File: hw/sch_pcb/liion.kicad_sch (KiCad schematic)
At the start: 67 parts, among them Q4 BC817-25, Q7 BSS83P, U1 BQ34Z100, U13 BQ25628E, U2 SN74HC164P

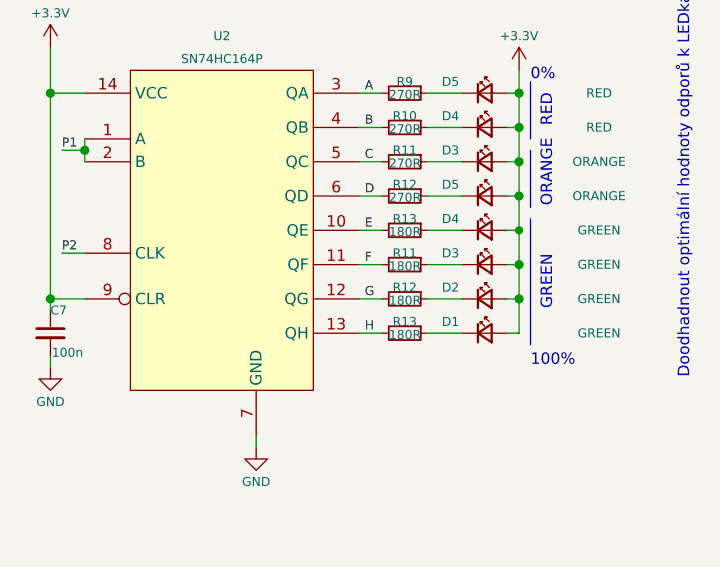
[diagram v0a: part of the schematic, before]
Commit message: Update components values to tested ones.
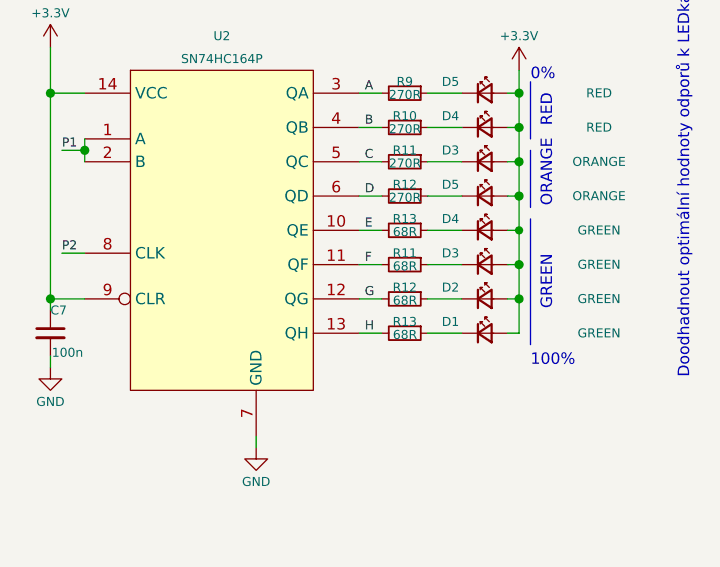
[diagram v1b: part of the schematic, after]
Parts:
- R11, R12, R13: value 180R -> 68R; UST_ID 5c70984512875079b91f897c -> 5c70984512875079b91f8975
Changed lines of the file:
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@@
       (effects (font (size 1 1)))
     )
-    (property "Value" "180R" (at 245.1354 130.9878 90)
+    (property "Value" "68R" (at 245.1354 130.9878 90)
       (effects (font (size 1 1)))
     )
@@
       (effects (font (size 1 1)) hide)
     )
-    (property "UST_ID" "5c70984512875079b91f897c" (at 245.11 130.81 0)
+    (property "UST_ID" "5c70984512875079b91f8975" (at 245.11 130.81 0)
       (effects (font (size 1.27 1.27)) hide)
     )
@@
       (effects (font (size 1 1)))
     )
-    (property "Value" "180R" (at 245.1354 134.7978 90)
+    (property "Value" "68R" (at 245.1354 134.7978 90)
       (effects (font (size 1 1)))
     )
@@
       (effects (font (size 1 1)) hide)
     )
-    (property "UST_ID" "5c70984512875079b91f897c" (at 245.11 134.62 0)
+    (property "UST_ID" "5c70984512875079b91f8975" (at 245.11 134.62 0)
       (effects (font (size 1.27 1.27)) hide)
     )
@@
       (effects (font (size 1 1)))
     )
-    (property "Value" "180R" (at 245.1354 142.4178 90)
+    (property "Value" "68R" (at 245.1354 142.4178 90)
       (effects (font (size 1 1)))
     )
@@
       (effects (font (size 1 1)) hide)
     )
-    (property "UST_ID" "5c70984512875079b91f897c" (at 245.11 142.24 0)
+    (property "UST_ID" "5c70984512875079b91f8975" (at 245.11 142.24 0)
       (effects (font (size 1.27 1.27)) hide)
     )
@@
       (effects (font (size 1 1)))
     )
-    (property "Value" "180R" (at 245.1354 138.6078 90)
+    (property "Value" "68R" (at 245.1354 138.6078 90)
       (effects (font (size 1 1)))
     )
@@
       (effects (font (size 1 1)) hide)
     )
-    (property "UST_ID" "5c70984512875079b91f897c" (at 245.11 138.43 0)
+    (property "UST_ID" "5c70984512875079b91f8975" (at 245.11 138.43 0)
       (effects (font (size 1.27 1.27)) hide)
     )

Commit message: Fix UST_ID.
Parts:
- R51: value 270R -> 68R; UST_ID 5c70984512875079b91f8983 -> 5c70984512875079b91f8975
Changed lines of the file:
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@@
       (effects (font (size 1 1)))
     )
-    (property "Value" "270R" (at 46.99 86.36 90)
+    (property "Value" "68R" (at 46.99 86.36 90)
       (effects (font (size 1 1)))
     )
@@
       (effects (font (size 1 1)) hide)
     )
-    (property "UST_ID" "5c70984512875079b91f8983" (at 46.99 86.36 0)
+    (property "UST_ID" "5c70984512875079b91f8975" (at 46.99 86.36 0)
       (effects (font (size 1.27 1.27)) hide)
     )

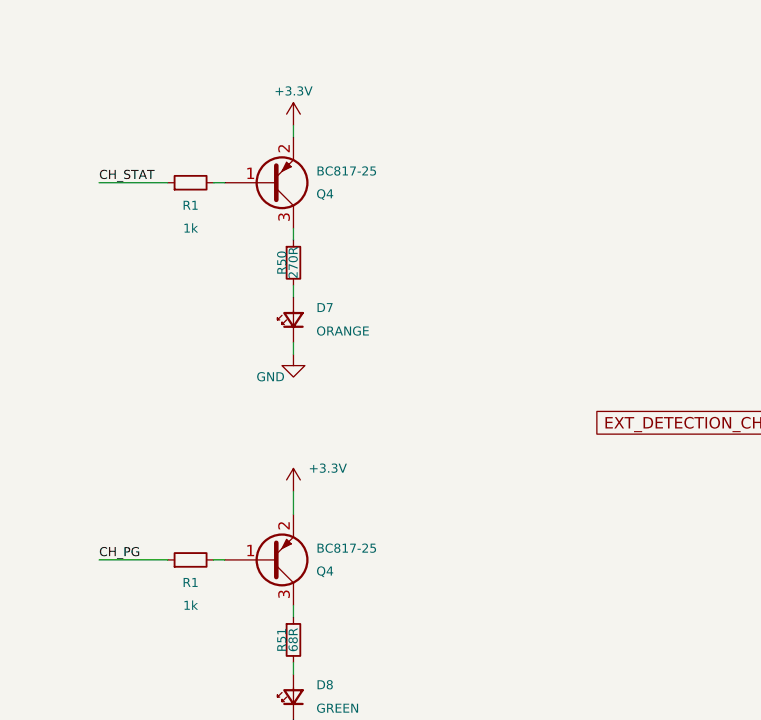
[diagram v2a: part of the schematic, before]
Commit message: Update and correct values from manufacturing process.
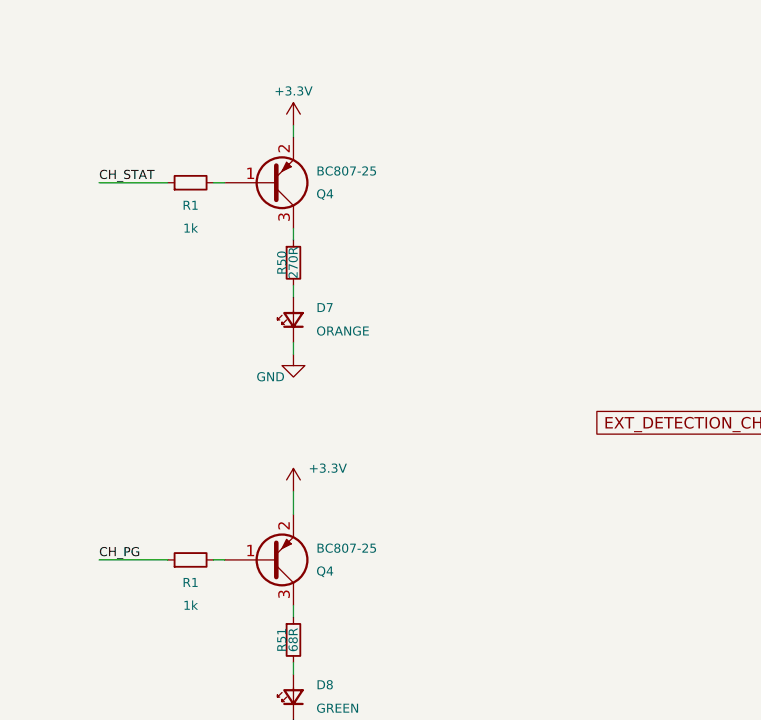
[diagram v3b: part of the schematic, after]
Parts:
- Q4: value BC817-25 -> BC807-25
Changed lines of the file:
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@@
       (effects (font (size 1 1)) (justify left))
     )
-    (property "Value" "BC817-25" (at 49.53 76.2 0)
+    (property "Value" "BC807-25" (at 49.53 76.2 0)
       (effects (font (size 1 1)) (justify left))
     )
@@
       (effects (font (size 1 1)) (justify left))
     )
-    (property "Value" "BC817-25" (at 49.53 34.29 0)
-      (effects (font (size 1 1)) (justify left))
-    )
+    (property "Value" "BC807-25" (at 49.53 34.29 0)
+      (effects (font (size 1 1)) (justify left))
+    )

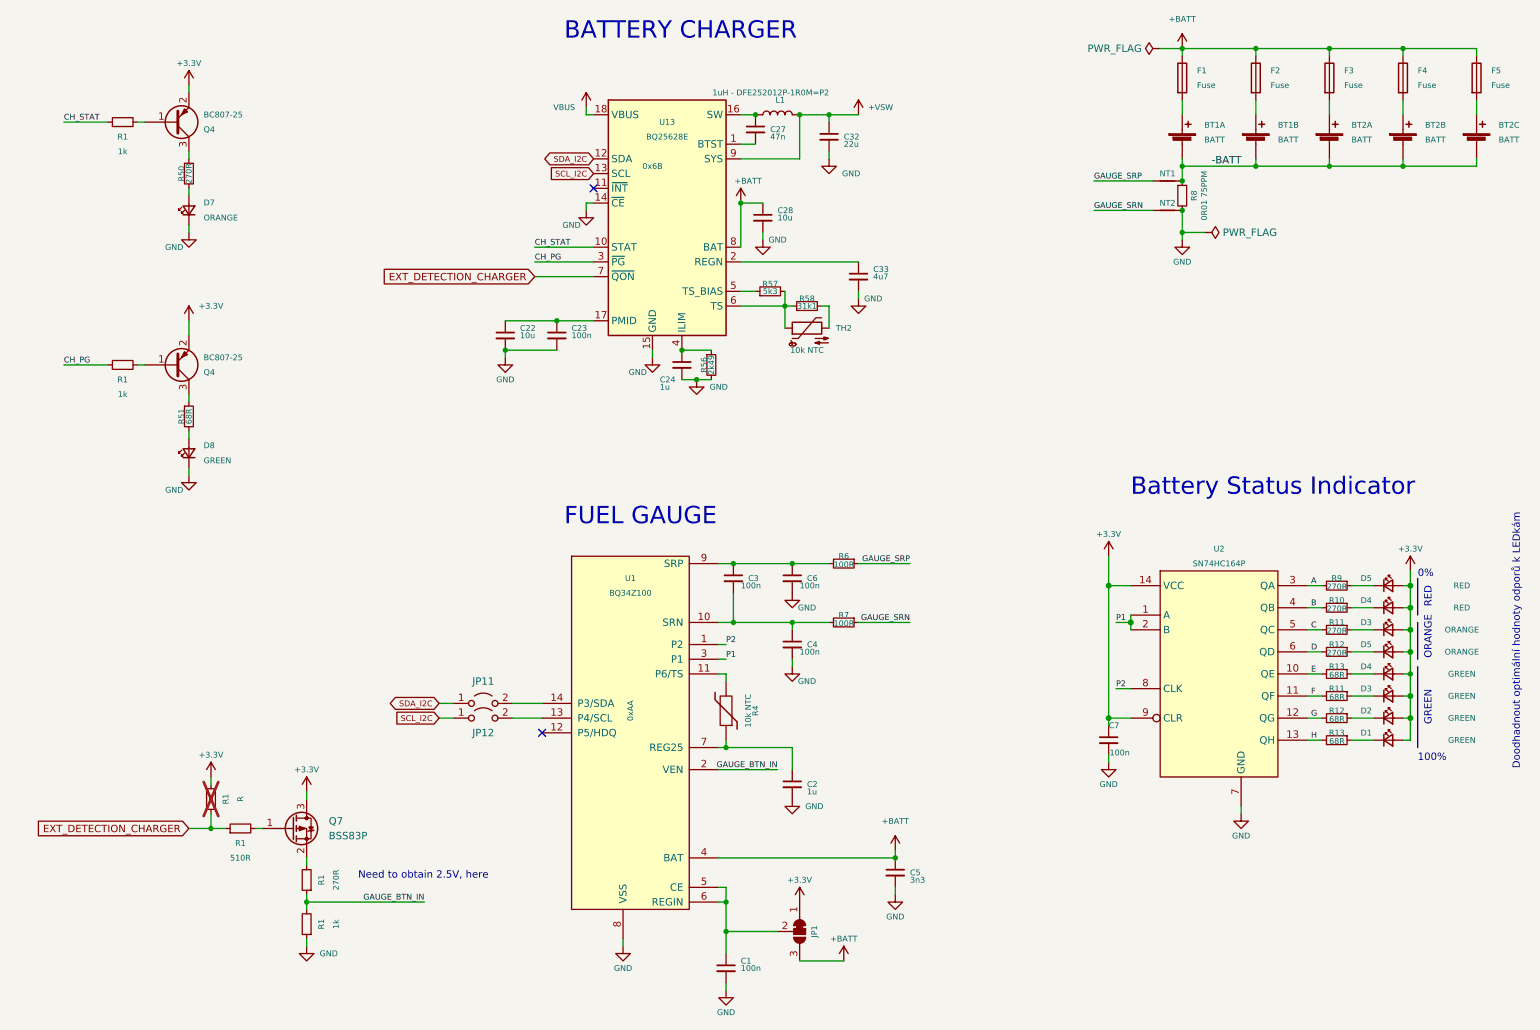
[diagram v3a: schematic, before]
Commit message: Update the commponent values according to actual component values used during manufacturing.
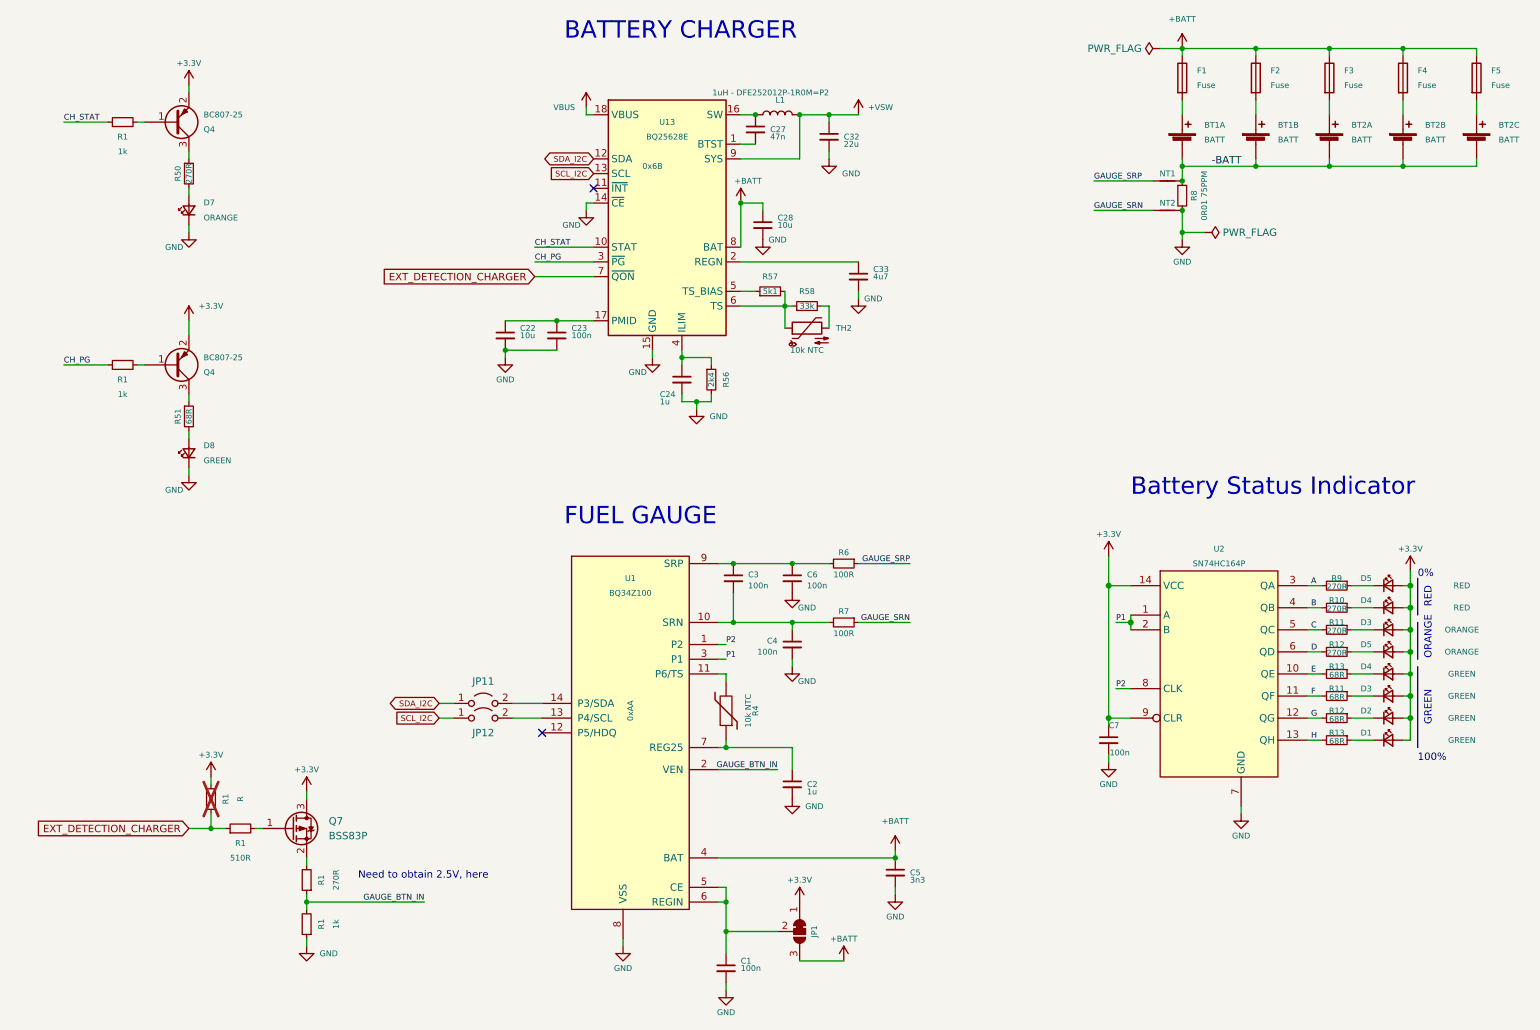
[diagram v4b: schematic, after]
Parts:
- R56: value 2k49 -> 2k4
- R57: value 5k3 -> 5k1
- R58: value 31k1 -> 33k
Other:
- note removed: "Doodhadnout optimální hodnoty odporů k LEDkám"
- company: MLAB.cz -> MLAB.cz, roman-dvorak
- moved on the sheet: C24, C28, R56
